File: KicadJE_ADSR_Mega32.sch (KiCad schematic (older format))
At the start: 57 parts, among them J101 ADSR1, J102 ADSR2, J103 ADSR1, J104 ADSR2, J105 ADSR1-G8, J106 ADSR2-G8, J107 ADSR4-G8, J108 ADSR3-G8, P101 Doepfer_Power_16pin

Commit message: Updating Atmega32A subboard
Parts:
- renumbered P101 to P?
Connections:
- net labels added: A0, A1, A2, A3, A4, A5, A6, A7
- net labels removed: +12V
- wire segments 123 -> 131
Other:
- moved on the sheet: RV101, RV102, RV103, RV104, RV105, RV106

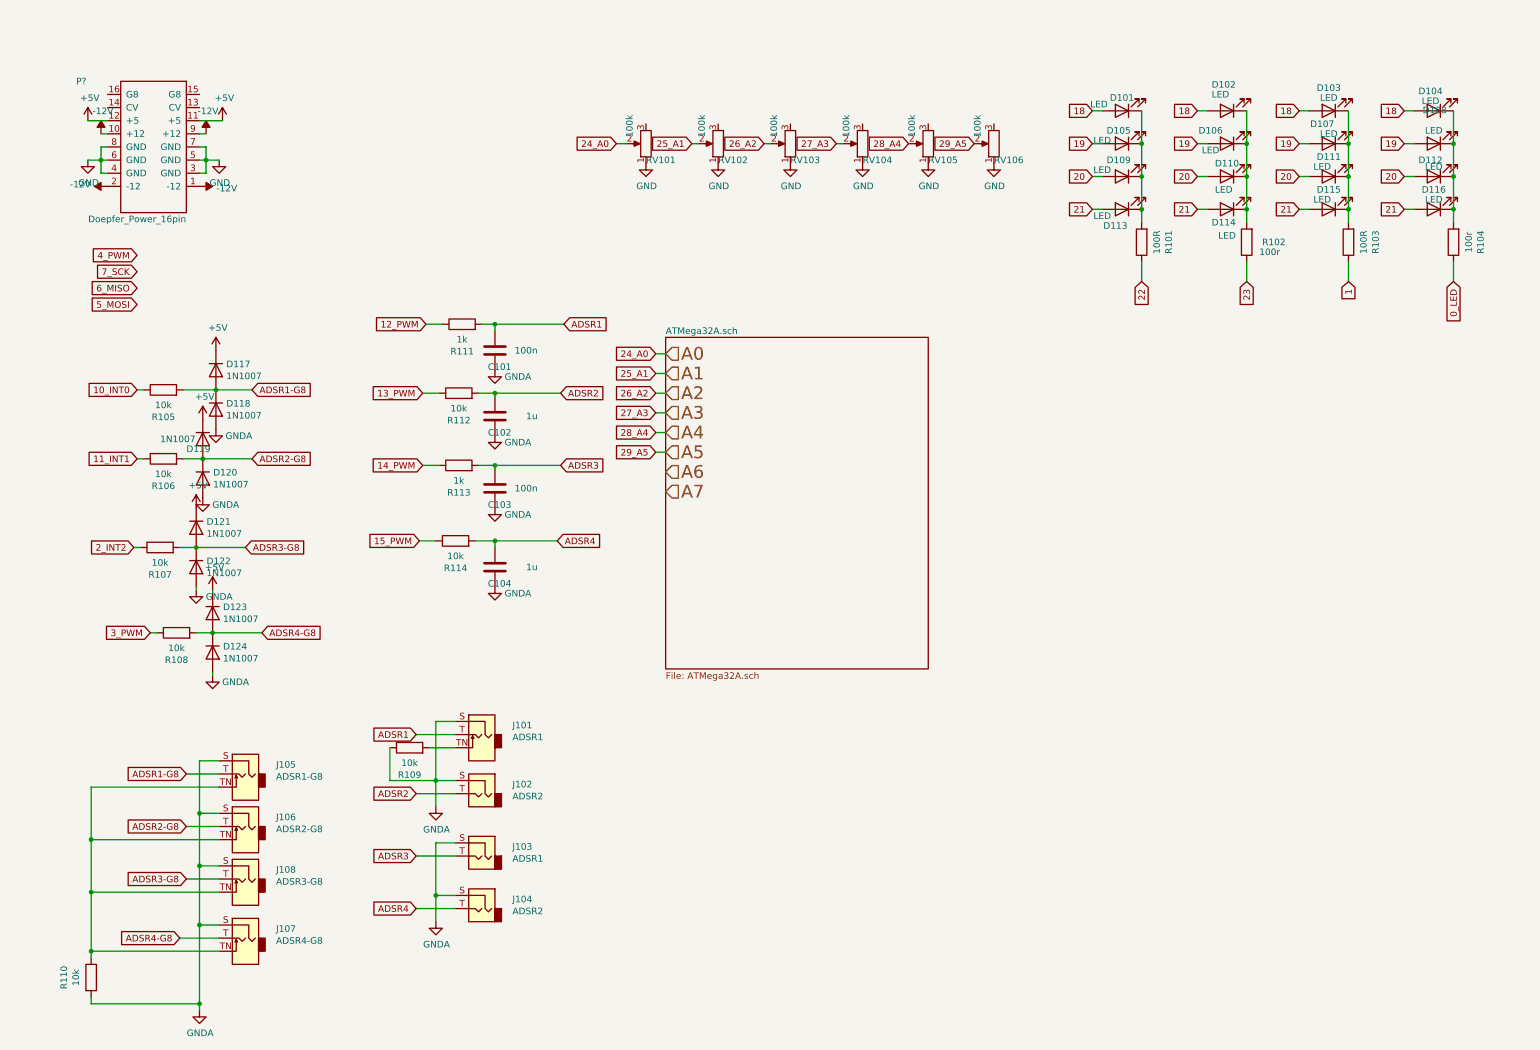
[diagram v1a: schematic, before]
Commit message: Placing hierarchical labels on ATMega32A
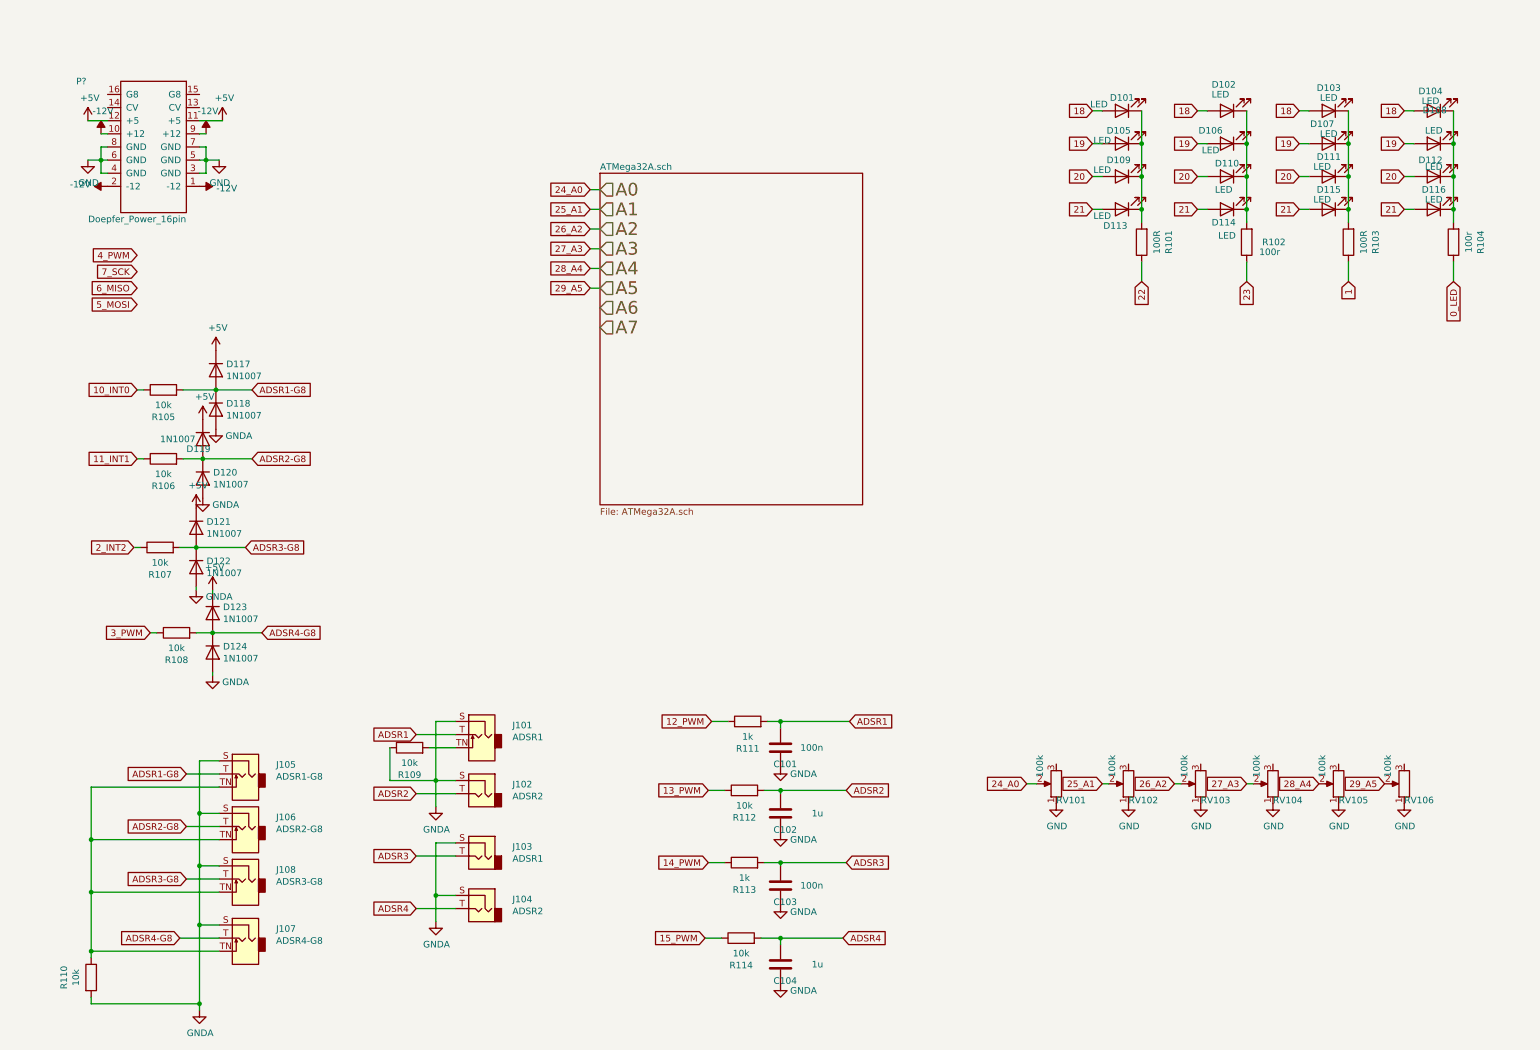
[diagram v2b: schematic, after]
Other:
- moved on the sheet: C101, C102, C103, C104, R111, R112, R113, R114, RV101, RV102, RV103, RV104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

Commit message: Subboard done
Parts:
- added C? (x2): 100n, Capacitor_SMD:C_0805_2012Metric_Pad1.15x1.40mm_HandSolder, symbol Device:C
- added C? (x3): 1u, Capacitor_SMD:C_1206_3216Metric_Pad1.42x1.75mm_HandSolder, symbol Device:C
- added D?: LED, AJ:D_0805_AJ, symbol Device:LED
- added J?: Conn_01x04_Female, symbol Connector:Conn_01x04_Female
- added R?: 22k, Resistor_SMD:R_0805_2012Metric_Pad1.15x1.40mm_HandSolder, symbol Device:R
- added R? (x3): 10R, Resistor_SMD:R_0805_2012Metric_Pad1.15x1.40mm_HandSolder, symbol Device:R
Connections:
- net +5V: now also RV101.3, RV102.3, RV103.3, RV104.3, RV105.3, RV106.3, C?.2, R?.2; no longer P?.11 (+5), P?.12 (+5)
- net -12V: now also C?.2, C?.2, R?.2, R?.2; no longer P?.1 (-12), P?.10 (+12), P?.2 (-12), P?.9 (+12)
- net GND: now also C?.1, C?.1, C?.1, C?.1, C?.1, D?.2 (A)
- new net: P?.1 (-12), P?.2 (-12), R?.1
- new net: P?.10 (+12), P?.9 (+12), R?.1
- new net: P?.11 (+5), P?.12 (+5), R?.1
- new net: D?.1 (K), R?.1
- new net +12V: C?.2, C?.2, R?.2

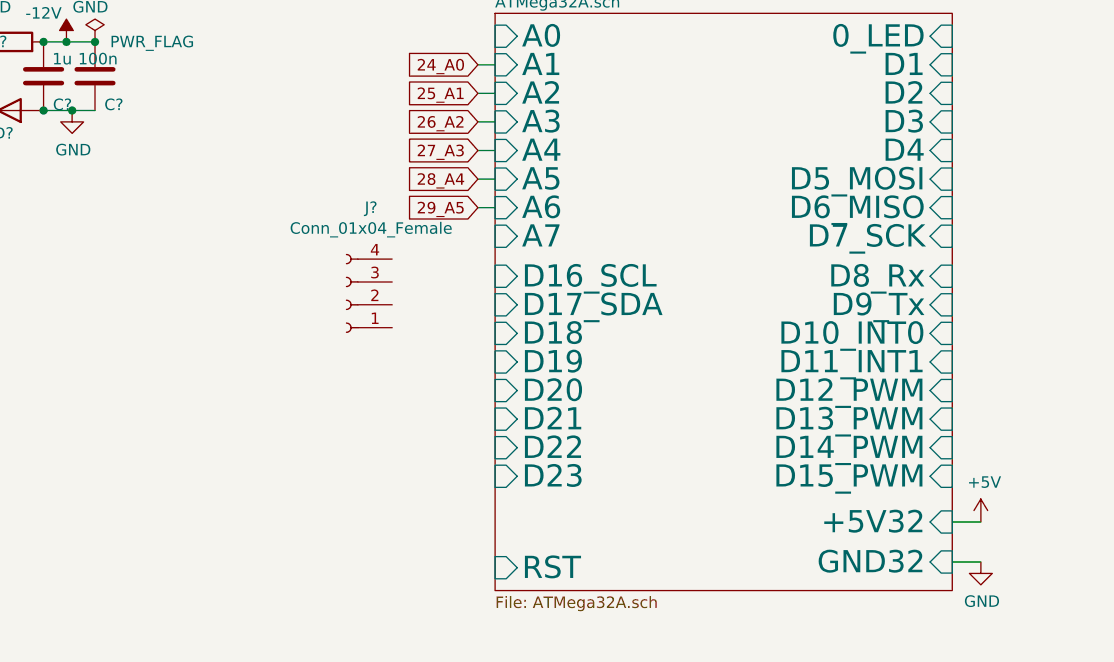
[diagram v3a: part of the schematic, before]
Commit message: Aref resolved - OLED in sch
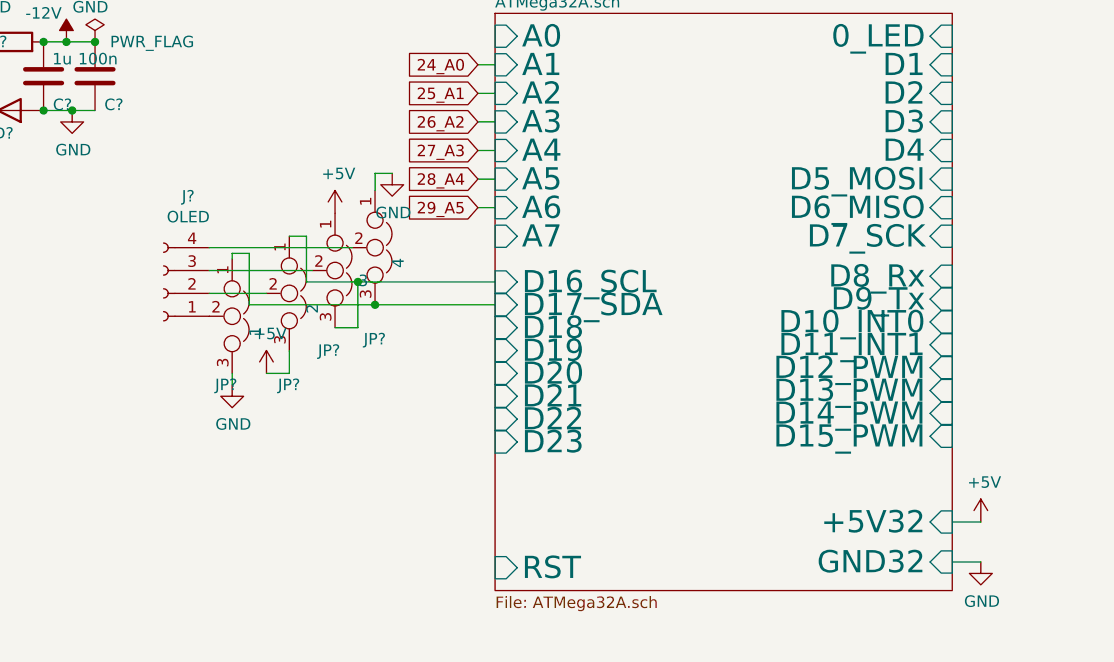
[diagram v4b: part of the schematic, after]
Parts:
- added JP?: 1, Jumper:SolderJumper-3_P1.3mm_Bridged12_Pad1.0x1.5mm_NumberLabels, symbol Device:Jumper_NC_Dual
- added JP?: 2, Jumper:SolderJumper-3_P1.3mm_Bridged12_Pad1.0x1.5mm_NumberLabels, symbol Device:Jumper_NC_Dual
- added JP?: 3, Jumper:SolderJumper-3_P1.3mm_Bridged12_Pad1.0x1.5mm_NumberLabels, symbol Device:Jumper_NC_Dual
- added JP?: 4, Jumper:SolderJumper-3_P1.3mm_Bridged12_Pad1.0x1.5mm_NumberLabels, symbol Device:Jumper_NC_Dual
- J?: value Conn_01x04_Female -> OLED
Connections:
- net +5V: now also JP?.1, JP?.3
- net ATMega32A.sch/D16_SCL: now also JP?.1, JP?.3
- net ATMega32A.sch/D17_SDA: now also JP?.1, JP?.3
- net GND: now also JP?.1, JP?.3
- net at J?.1 (Pin_1): now also JP?.2
- net at J?.2 (Pin_2): now also JP?.2
- net at J?.3 (Pin_3): now also JP?.2
- net at J?.4 (Pin_4): now also JP?.2
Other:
- moved on the sheet: J?
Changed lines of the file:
@@
 F17 "D7_SCK" I R 6500 2100 97
 F18 "RST" I L 4500 3550 97
-F19 "D16_SCL" I L 4500 2275 97
+F19 "D16_SCL" I L 4500 2300 97
 F20 "D17_SDA" I L 4500 2400 97
-F21 "D18" I L 4500 2525 97
-F22 "D19" I L 4500 2650 97
-F23 "D20" I L 4500 2775 97
-F24 "D21" I L 4500 2900 97
-F25 "D22" I L 4500 3025 97
-F26 "D23" I L 4500 3150 97
+F21 "D18" I L 4500 2500 97
+F22 "D19" I L 4500 2600 97
+F23 "D20" I L 4500 2700 97
+F24 "D21" I L 4500 2800 97
+F25 "D22" I L 4500 2900 97
+F26 "D23" I L 4500 3000 97
 F27 "D8_Rx" I R 6500 2275 97
-F28 "D9_Tx" I R 6500 2400 97
-F29 "D12_PWM" I R 6500 2775 97
-F30 "D13_PWM" I R 6500 2900 97
-F31 "D14_PWM" I R 6500 3025 97
-F32 "D15_PWM" I R 6500 3150 97
-F33 "D10_INT0" I R 6500 2525 97
-F34 "D11_INT1" I R 6500 2650 97
+F28 "D9_Tx" I R 6500 2375 97
+F29 "D12_PWM" I R 6500 2675 97
+F30 "D13_PWM" I R 6500 2775 97
+F31 "D14_PWM" I R 6500 2875 97
+F32 "D15_PWM" I R 6500 2975 97
+F33 "D10_INT0" I R 6500 2475 97
+F34 "D11_INT1" I R 6500 2575 97
 F35 "+5V32" I R 6500 3350 97
 F36 "GND32" I R 6500 3525 97
@@
 L Connector:Conn_01x04_Female J?
 U 1 1 60BF44F5
-P 3850 2400
-F 0 "J?" H 3742 1975 50  0000 C CNN
-F 1 "Conn_01x04_Female" H 3742 2066 50  0000 C CNN
-F 2 "" H 3850 2400 50  0001 C CNN
-F 3 "~" H 3850 2400 50  0001 C CNN
-	1    3850 2400
-	-1   0    0    1
-$EndComp
+P 3050 2350
+F 0 "J?" H 2942 1925 50  0000 C CNN
+F 1 "OLED" H 2942 2016 50  0000 C CNN
+F 2 "" H 3050 2350 50  0001 C CNN
+F 3 "~" H 3050 2350 50  0001 C CNN
+	1    3050 2350
+	-1   0    0    1
+$EndComp
+$Comp
+L power:GND #PWR?
+U 1 1 60C01EFA
+P 4050 1825
+AR Path="/608CA457/60C01EFA" Ref="#PWR?"  Part="1"
+AR Path="/608CA457/5CD3F059/60C01EFA" Ref="#PWR?"  Part="1"
+F 0 "#PWR?" H 4050 1575 50  0001 C CNN
+F 1 "GND" H 4055 1652 50  0000 C CNN
+F 2 "" H 4050 1825 50  0001 C CNN
+F 3 "" H 4050 1825 50  0001 C CNN
+	1    4050 1825
+	1    0    0    -1
+$EndComp
+$Comp
+L power:+5V #PWR?
+U 1 1 60C0BC24
+P 3800 2000
+F 0 "#PWR?" H 3800 1850 50  0001 C CNN
+F 1 "+5V" H 3815 2173 50  0000 C CNN
+F 2 "" H 3800 2000 50  0001 C CNN
+F 3 "" H 3800 2000 50  0001 C CNN
+	1    3800 2000
+	1    0    0    -1
+$EndComp
+$Comp
+L Device:Jumper_NC_Dual JP?
+U 1 1 60CA048D
+P 3350 2450
+F 0 "JP?" V 3650 2375 50  0000 L CNN
+F 1 "1" H 3395 2552 50  0000 L CNN
+F 2 "Jumper:SolderJumper-3_P1.3mm_Bridged12_Pad1.0x1.5mm_NumberLabels" H 3350 2450 50  0001 C CNN
+F 3 "~" H 3350 2450 50  0001 C CNN
+	1    3350 2450
+	0    1    1    0
+$EndComp
+Wire Wire Line
+	3250 2250 3700 2250
+Wire Wire Line
+	3250 2350 3500 2350
+$Comp
+L Device:Jumper_NC_Dual JP?
+U 1 1 60CD1C03
+P 3600 2350
+F 0 "JP?" V 4000 2300 50  0000 L CNN
+F 1 "2" H 3645 2452 50  0000 L CNN
+F 2 "Jumper:SolderJumper-3_P1.3mm_Bridged12_Pad1.0x1.5mm_NumberLabels" H 3600 2350 50  0001 C CNN
+F 3 "~" H 3600 2350 50  0001 C CNN
+	1    3600 2350
+	0    1    1    0
+$EndComp
+$Comp
+L Device:Jumper_NC_Dual JP?
+U 1 1 60CD20EB
+P 3800 2250
+F 0 "JP?" V 4150 2175 50  0000 L CNN
+F 1 "3" V 3845 2352 50  0000 L CNN
+F 2 "Jumper:SolderJumper-3_P1.3mm_Bridged12_Pad1.0x1.5mm_NumberLabels" H 3800 2250 50  0001 C CNN
+F 3 "~" H 3800 2250 50  0001 C CNN
+	1    3800 2250
+	0    1    1    0
+$EndComp
+Wire Wire Line
+	3250 2150 3875 2150
+$Comp
+L Device:Jumper_NC_Dual JP?
+U 1 1 60CD252A
+P 3975 2150
+F 0 "JP?" V 4375 2100 50  0000 L CNN
+F 1 "4" H 4020 2252 50  0000 L CNN
+F 2 "Jumper:SolderJumper-3_P1.3mm_Bridged12_Pad1.0x1.5mm_NumberLabels" H 3975 2150 50  0001 C CNN
+F 3 "~" H 3975 2150 50  0001 C CNN
+	1    3975 2150
+	0    1    1    0
+$EndComp
+Wire Wire Line
+	3975 1900 3975 1825
+Wire Wire Line
+	3975 1825 4050 1825
+$Comp
+L power:GND #PWR?
+U 1 1 60CF8E24
+P 3350 2750
+AR Path="/608CA457/60CF8E24" Ref="#PWR?"  Part="1"
+AR Path="/608CA457/5CD3F059/60CF8E24" Ref="#PWR?"  Part="1"
+F 0 "#PWR?" H 3350 2500 50  0001 C CNN
+F 1 "GND" H 3355 2577 50  0000 C CNN
+F 2 "" H 3350 2750 50  0001 C CNN
+F 3 "" H 3350 2750 50  0001 C CNN
+	1    3350 2750
+	1    0    0    -1
+$EndComp
+$Comp
+L power:+5V #PWR?
+U 1 1 60CF91B4
+P 3500 2700
+F 0 "#PWR?" H 3500 2550 50  0001 C CNN
+F 1 "+5V" H 3515 2873 50  0000 C CNN
+F 2 "" H 3500 2700 50  0001 C CNN
+F 3 "" H 3500 2700 50  0001 C CNN
+	1    3500 2700
+	1    0    0    -1
+$EndComp
+Wire Wire Line
+	3500 2700 3600 2700
+Wire Wire Line
+	3600 2700 3600 2600
+Wire Wire Line
+	3350 2750 3350 2700
+Wire Wire Line
+	3675 2300 3675 2100
+Wire Wire Line
+	3675 2100 3600 2100
+Wire Wire Line
+	3675 2300 3900 2300
+Wire Wire Line
+	3975 2400 4500 2400
+Wire Wire Line
+	3975 2400 3425 2400
+Wire Wire Line
+	3425 2400 3425 2175
+Wire Wire Line
+	3425 2175 3350 2175
+Wire Wire Line
+	3350 2175 3350 2200
+Connection ~ 3975 2400
+Wire Wire Line
+	3800 2500 3900 2500
+Wire Wire Line
+	3900 2500 3900 2300
+Connection ~ 3900 2300
+Wire Wire Line
+	3900 2300 4500 2300
 $EndSCHEMATC

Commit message: Front LED
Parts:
- removed C103: 100n, Capacitor_SMD:C_0805_2012Metric_Pad1.15x1.40mm_HandSolder, symbol Device:C
- removed C104: 1u, Capacitor_SMD:C_0805_2012Metric_Pad1.15x1.40mm_HandSolder, symbol Device:C
- removed D101, D102, D103, D104, D105, D106, D107, D108, D109, D110, D111, D112, D113, D114, D115, D116: LED, LED_THT:LED_D3.0mm, symbol Device:LED
- removed J103: ADSR1, AJ-Dropbox-Kicad:PJ301SM, symbol Connector:AudioJack2
- removed J104: ADSR2, AJ-Dropbox-Kicad:PJ301SM, symbol Connector:AudioJack2
- removed R101, R103: 100R, Resistor_SMD:R_0805_2012Metric_Pad1.15x1.40mm_HandSolder, symbol Device:R
- removed R102, R104: 100r, Resistor_SMD:R_0805_2012Metric_Pad1.15x1.40mm_HandSolder, symbol Device:R
- removed R113: 1k, Resistor_SMD:R_0805_2012Metric_Pad1.15x1.40mm_HandSolder, symbol Device:R
- removed R114: 10k, Resistor_SMD:R_0805_2012Metric_Pad1.15x1.40mm_HandSolder, symbol Device:R
- removed RV101, RV102, RV103, RV104, RV105, RV106: 100k, Potentiometer_THT:Potentiometer_China_RK09_Single_Vertical_AJ, symbol Device:R_POT
- added J?: FrontLED, Connector_PinSocket_2.54mm:PinSocket_1x06_P2.54mm_Vertical, symbol Connector:Conn_01x06_Female
- J?: footprint (none) -> Connector_PinSocket_2.54mm:PinSocket_1x04_P2.54mm_Vertical
- R109: value 10k -> OPEN
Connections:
- net labels added: CV1, CV2, In1, In2, Out1, Out2
- net labels removed: 0_LED, 1, 14_PWM, 15_PWM, 18, 19, 20, 21, 22, 23, ADSR1-G8, ADSR2-G8, ADSR3, ADSR3-G8, ADSR4, ADSR4-G8
- wire segments 185 -> 141
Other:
- moved on the sheet: C101, C102, R111, R112

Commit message: Cleanup MasterSCH
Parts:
- removed J101: ADSR1, AJ-Dropbox-Kicad:PJ301SM, symbol Connector:AudioJack2_SwitchT
- removed R109: OPEN, Resistor_SMD:R_0805_2012Metric_Pad1.15x1.40mm_HandSolder, symbol Device:R
- removed R110: 10k, Resistor_SMD:R_0805_2012Metric_Pad1.15x1.40mm_HandSolder, symbol Device:R
- added C? (x2): 100n, AJ:C_0805_AJ, symbol Device:C
- added C? (x2): 0R, AJ:C_0805_AJ, symbol Device:C
- added J?: OUT1, AJ-Dropbox-Kicad:PJ301SM, symbol Connector:AudioJack2
- added J?: Input, Connector_PinSocket_2.54mm:PinSocket_1x06_P2.54mm_Vertical, symbol Connector:Conn_01x06_Female
- added J?: Out1, Connector_PinSocket_2.54mm:PinSocket_1x02_P2.54mm_Vertical, symbol Connector:Conn_01x02_Female
- added J?: Out2, Connector_PinSocket_2.54mm:PinSocket_1x02_P2.54mm_Vertical, symbol Connector:Conn_01x02_Female
- added J?: -12V Front, Connector_PinSocket_2.54mm:PinSocket_1x02_P2.54mm_Vertical, symbol Connector:Conn_01x02_Female
- added R? (x4): 1k, Resistor_SMD:R_0805_2012Metric_Pad1.15x1.40mm_HandSolder, symbol Device:R
- added R? (x6): 20k, Resistor_SMD:R_0805_2012Metric_Pad1.15x1.40mm_HandSolder, symbol Device:R
- added R? (x4): 10R, Resistor_SMD:R_0805_2012Metric_Pad1.15x1.40mm_HandSolder, symbol Device:R
- added R? (x2): OPEN, Resistor_SMD:R_0805_2012Metric_Pad1.15x1.40mm_HandSolder, symbol Device:R
- added TP?: Flow1, TestPoint:TestPoint_THTPad_2.0x2.0mm_Drill1.0mm, symbol Connector:TestPoint
- added TP?: Flow2, TestPoint:TestPoint_THTPad_2.0x2.0mm_Drill1.0mm, symbol Connector:TestPoint
- added U? (x3): TL072, AJ-Dropbox-Kicad:AJ_SO-8_5.3x6.2mm_P1.27mm, symbol Amplifier_Operational:TL072
- C101, C102: footprint Capacitor_SMD:C_0805_2012Metric_Pad1.15x1.40mm_HandSolder -> Capacitor_SMD:C_1206_3216Metric
- C? (x2): footprint Capacitor_SMD:C_0805_2012Metric_Pad1.15x1.40mm_HandSolder -> AJ:C_0805_AJ
- C? (x3): footprint Capacitor_SMD:C_1206_3216Metric_Pad1.42x1.75mm_HandSolder -> AJ:C_0805_AJ
- J102: value ADSR2 -> OUT2
- J105: value ADSR1-G8 -> IN1
- J106: value ADSR2-G8 -> IN2
- J107: value ADSR4-G8 -> CV2
- J108: value ADSR3-G8 -> CV1
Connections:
- net labels added: CV1_32, CV2_32, Flow1_32, Flow2_32, In1_32, In2_32, Out1_32, Out2_32
- net labels removed: 12_PWM, 13_PWM, ADSR1, ADSR2, CV1, CV2, In1, In2, Out1, Out2
- wire segments 141 -> 190
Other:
- moved on the sheet: C101, C102, C?, D117, D118, D119, D120, D121, D122, D123, D124, D?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
